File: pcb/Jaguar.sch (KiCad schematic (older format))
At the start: 52 parts

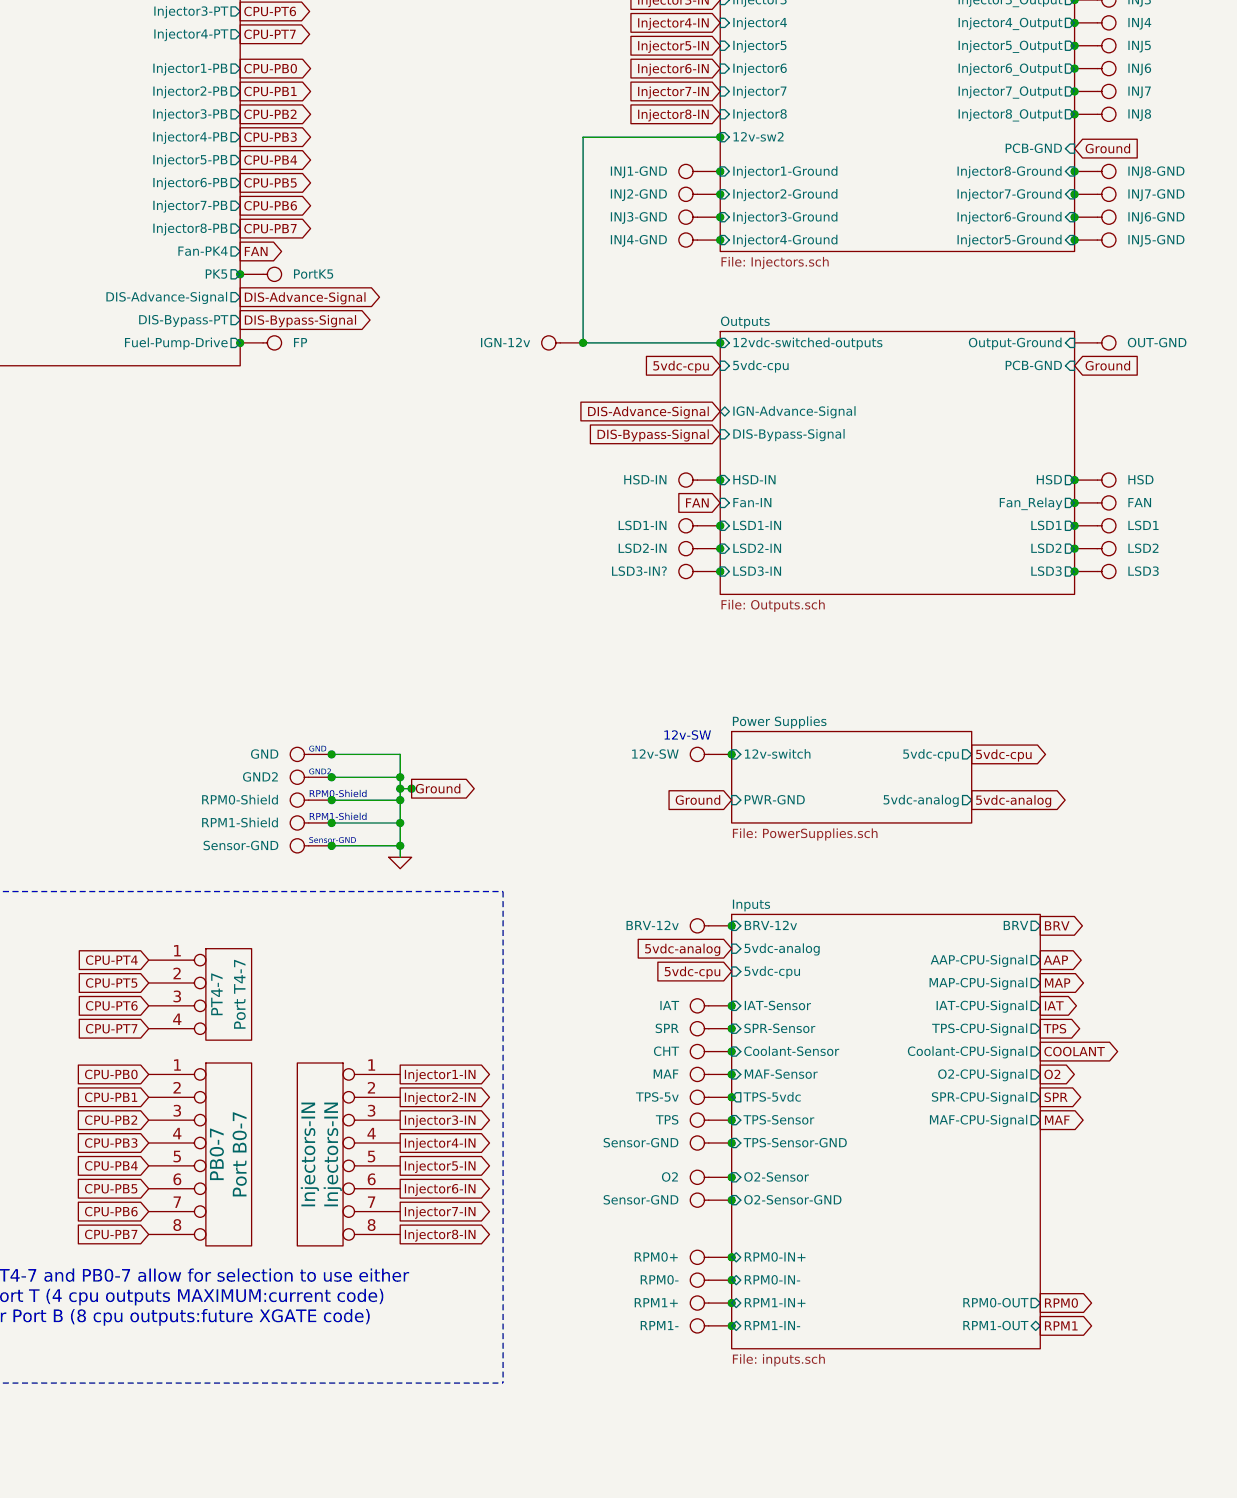
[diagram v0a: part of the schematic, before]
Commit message: Started laying out PCB changes for SO-8 high side driver and new SO-8 low side drivers.
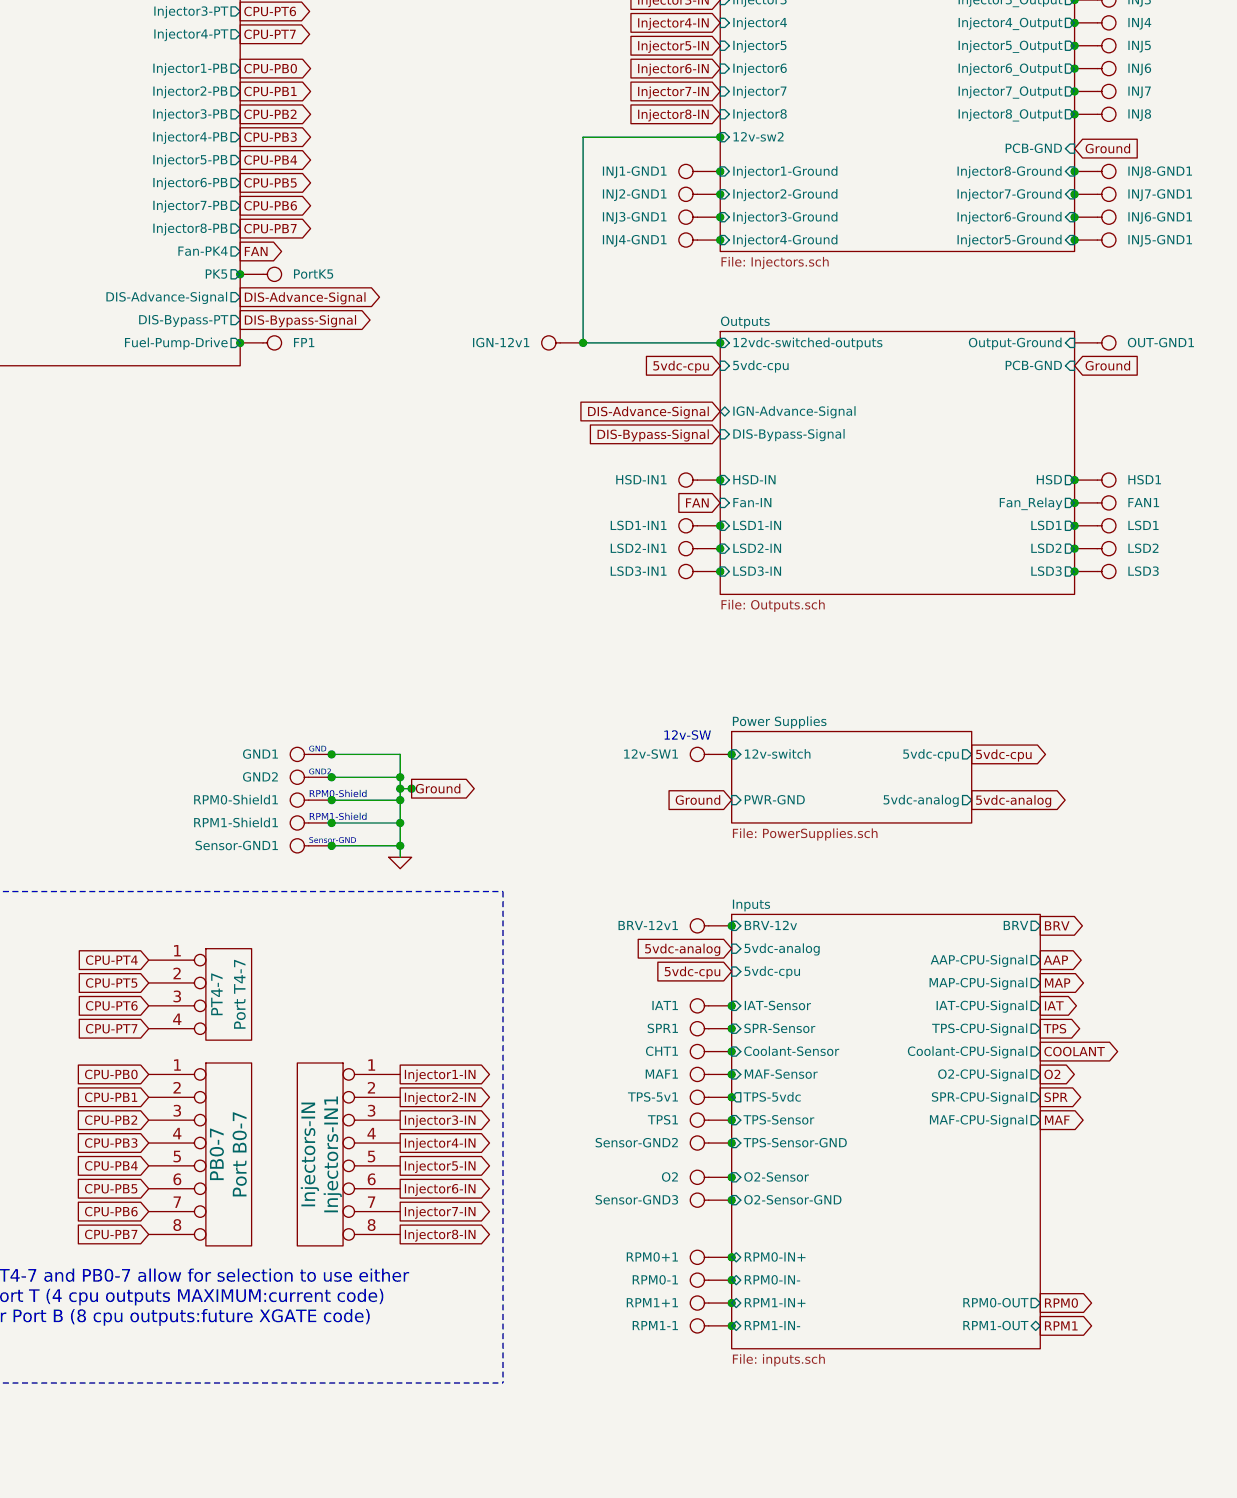
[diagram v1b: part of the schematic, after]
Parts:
- gave numbers to parts that had none: 1
- renumbered 12v-SW to 12v-SW1, BRV-12v to BRV-12v1, CHT to CHT1, FAN to FAN1, FP to FP1, GND to GND1, HSD-IN to HSD-IN1, HSD to HSD1, IAT to IAT1, IGN-12v to IGN-12v1, INJ1-GND to INJ1-GND1, INJ2-GND to INJ2-GND1, INJ3-GND to INJ3-GND1, INJ4-GND to INJ4-GND1, INJ5-GND to INJ5-GND1, INJ6-GND to INJ6-GND1, INJ7-GND to INJ7-GND1, INJ8-GND to INJ8-GND1, Injectors-IN to Injectors-IN1, LSD1-IN to LSD1-IN1, LSD2-IN to LSD2-IN1, MAF to MAF1, OUT-GND to OUT-GND1, RPM0+ to RPM0+1, RPM0- to RPM0-1, RPM0-Shield to RPM0-Shield1, RPM1+ to RPM1+1, RPM1- to RPM1-1, RPM1-Shield to RPM1-Shield1, SPR to SPR1, Sensor-GND to Sensor-GND1, Sensor-GND to Sensor-GND2, Sensor-GND to Sensor-GND3, TPS-5v to TPS-5v1, TPS to TPS1
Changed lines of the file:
@@
 Sheet 1 7
 Title "Jaguar PCB for FreeEMS"
-Date "5 feb 2014"
+Date "4 mar 2014"
 Rev "0.7-alpha"
 Comp "Git: xxxxxxxxxx"
@@
 MAF
 $Comp
-L CONN_1 INJ8-GND
+L CONN_1 INJ8-GND1
 U 1 1 4FF7159F
 P 10700 1650
-F 0 "INJ8-GND" H 10780 1650 40  0000 L CNN
+F 0 "INJ8-GND1" H 10780 1650 40  0000 L CNN
 F 1 "INJ8-GND" H 10700 1705 30  0001 C CNN
 F 2 "" H 10700 1650 60  0001 C CNN
@@
 $EndComp
 $Comp
-L CONN_1 INJ7-GND
+L CONN_1 INJ7-GND1
 U 1 1 4FF7159C
 P 10700 1750
-F 0 "INJ7-GND" H 10780 1750 40  0000 L CNN
+F 0 "INJ7-GND1" H 10780 1750 40  0000 L CNN
 F 1 "INJ7-GND" H 10700 1805 30  0001 C CNN
 F 2 "" H 10700 1750 60  0001 C CNN
@@
 $EndComp
 $Comp
-L CONN_1 INJ6-GND
+L CONN_1 INJ6-GND1
 U 1 1 4FF71599
 P 10700 1850
-F 0 "INJ6-GND" H 10780 1850 40  0000 L CNN
+F 0 "INJ6-GND1" H 10780 1850 40  0000 L CNN
 F 1 "INJ6-GND" H 10700 1905 30  0001 C CNN
 F 2 "" H 10700 1850 60  0001 C CNN
@@
 $EndComp
 $Comp
-L CONN_1 INJ5-GND
+L CONN_1 INJ5-GND1
 U 1 1 4FF71591
 P 10700 1950
-F 0 "INJ5-GND" H 10780 1950 40  0000 L CNN
+F 0 "INJ5-GND1" H 10780 1950 40  0000 L CNN
 F 1 "INJ5-GND" H 10700 2005 30  0001 C CNN
 F 2 "" H 10700 1950 60  0001 C CNN
@@
 $EndComp
 $Comp
-L CONN_1 INJ4-GND
+L CONN_1 INJ4-GND1
 U 1 1 4FF7158E
 P 8850 1950
-F 0 "INJ4-GND" H 8930 1950 40  0000 L CNN
+F 0 "INJ4-GND1" H 8930 1950 40  0000 L CNN
 F 1 "INJ4-GND" H 8850 2005 30  0001 C CNN
 F 2 "" H 8850 1950 60  0001 C CNN
@@
 $EndComp
 $Comp
-L CONN_1 INJ3-GND
+L CONN_1 INJ3-GND1
 U 1 1 4FF7158B
 P 8850 1850
-F 0 "INJ3-GND" H 8930 1850 40  0000 L CNN
+F 0 "INJ3-GND1" H 8930 1850 40  0000 L CNN
 F 1 "INJ3-GND" H 8850 1905 30  0001 C CNN
 F 2 "" H 8850 1850 60  0001 C CNN
@@
 5vdc-cpu = VDD\n\n5vdc-analog = VCC
 $Comp
-L CONN_1 Sensor-GND
+L CONN_1 Sensor-GND1
 U 1 1 4F2A0E57
 P 7150 4600
-F 0 "Sensor-GND" H 7230 4600 40  0000 L CNN
+F 0 "Sensor-GND1" H 7230 4600 40  0000 L CNN
 F 1 "Sensor-GND" H 7150 4655 30  0001 C CNN
 F 2 "" H 7150 4600 60  0001 C CNN
@@
 RPM0-Shield
 $Comp
-L CONN_1 RPM1-Shield
+L CONN_1 RPM1-Shield1
 U 1 1 4F2A0D57
 P 7150 4500
-F 0 "RPM1-Shield" H 7230 4500 40  0000 L CNN
+F 0 "RPM1-Shield1" H 7230 4500 40  0000 L CNN
 F 1 "RPM1-Shield" H 7150 4555 30  0001 C CNN
 F 2 "" H 7150 4500 60  0001 C CNN
@@
 $EndComp
 $Comp
-L CONN_1 RPM0-Shield
+L CONN_1 RPM0-Shield1
 U 1 1 4F2A0D4D
 P 7150 4400
-F 0 "RPM0-Shield" H 7230 4400 40  0000 L CNN
+F 0 "RPM0-Shield1" H 7230 4400 40  0000 L CNN
 F 1 "RPM0-Shield" H 7150 4455 30  0001 C CNN
 F 2 "" H 7150 4400 60  0001 C CNN
@@
 GND
 $Comp
-L CONN_1 INJ2-GND
+L CONN_1 INJ2-GND1
 U 1 1 4F2A047E
 P 8850 1750
-F 0 "INJ2-GND" H 8930 1750 40  0000 L CNN
+F 0 "INJ2-GND1" H 8930 1750 40  0000 L CNN
 F 1 "INJ2-GND" H 8850 1805 30  0001 C CNN
 F 2 "" H 8850 1750 60  0001 C CNN
@@
 $EndComp
 $Comp
-L CONN_1 MAF
+L CONN_1 MAF1
 U 1 1 4F22BF32
 P 8900 5600
-F 0 "MAF" H 8980 5600 40  0000 L CNN
+F 0 "MAF1" H 8980 5600 40  0000 L CNN
 F 1 "MAF" H 8900 5655 30  0001 C CNN
 F 2 "" H 8900 5600 60  0001 C CNN
@@
 $EndComp
 $Comp
-L CONN_1 LSD1-IN
+L CONN_1 LSD1-IN1
 U 1 1 4F2222E6
 P 8850 3200
-F 0 "LSD1-IN" H 8930 3200 40  0000 L CNN
+F 0 "LSD1-IN1" H 8930 3200 40  0000 L CNN
 F 1 "LSD1-IN" H 8850 3255 30  0001 C CNN
 F 2 "" H 8850 3200 60  0001 C CNN
@@
 $EndComp
 $Comp
-L CONN_1 LSD2-IN
+L CONN_1 LSD2-IN1
 U 1 1 4F2222DF
 P 8850 3300
-F 0 "LSD2-IN" H 8930 3300 40  0000 L CNN
+F 0 "LSD2-IN1" H 8930 3300 40  0000 L CNN
 F 1 "LSD2-IN" H 8850 3355 30  0001 C CNN
 F 2 "" H 8850 3300 60  0001 C CNN
@@
 Injector7-IN
 $Comp
-L CONN_8 Injectors-IN
+L CONN_8 Injectors-IN1
 U 1 1 4F20E01E
 P 7250 5950
-F 0 "Injectors-IN" V 7200 5950 60  0000 C CNN
+F 0 "Injectors-IN1" V 7200 5950 60  0000 C CNN
 F 1 "Injectors-IN" V 7300 5950 60  0000 C CNN
 F 2 "" H 7250 5950 60  0001 C CNN
@@
 Notes:
 $Comp
-L CONN_1 IGN-12v
+L CONN_1 IGN-12v1
 U 1 1 4F1CD4E4
 P 8250 2400
-F 0 "IGN-12v" H 8330 2400 40  0000 L CNN
+F 0 "IGN-12v1" H 8330 2400 40  0000 L CNN
 F 1 "IGN-12v" H 8250 2455 30  0001 C CNN
 F 2 "" H 8250 2400 60  0001 C CNN
@@
 $EndComp
 $Comp
-L CONN_1 OUT-GND
+L CONN_1 OUT-GND1
 U 1 1 4F1CD3BD
 P 10700 2400
-F 0 "OUT-GND" H 10780 2400 40  0000 L CNN
+F 0 "OUT-GND1" H 10780 2400 40  0000 L CNN
 F 1 "OUT-GND" H 10700 2455 30  0001 C CNN
 F 2 "" H 10700 2400 60  0001 C CNN
@@
 $EndComp
 $Comp
-L GND #PWR01
+L GND #PWR1
 U 1 1 4F1CCA54
 P 7600 4650
-F 0 "#PWR01" H 7600 4650 30  0001 C CNN
+F 0 "#PWR1" H 7600 4650 30  0001 C CNN
 F 1 "GND" H 7600 4580 30  0001 C CNN
 F 2 "" H 7600 4650 60  0001 C CNN
@@
 $EndComp
 $Comp
-L CONN_1 TPS-5v
+L CONN_1 TPS-5v1
 U 1 1 4F1CC8BD
 P 8900 5700
-F 0 "TPS-5v" H 8980 5700 40  0000 L CNN
+F 0 "TPS-5v1" H 8980 5700 40  0000 L CNN
 F 1 "TPS-5v" H 8900 5755 30  0001 C CNN
 F 2 "" H 8900 5700 60  0001 C CNN
@@
 5vdc-analog
 $Comp
-L CONN_1 GND
+L CONN_1 GND1
 U 1 1 4F189D7E
 P 7150 4200
-F 0 "GND" H 7230 4200 40  0000 L CNN
+F 0 "GND1" H 7230 4200 40  0000 L CNN
 F 1 "GND" H 7150 4255 30  0001 C CNN
 F 2 "" H 7150 4200 60  0001 C CNN
@@
 RPM1
 $Comp
-L CONN_1 RPM0-
+L CONN_1 RPM0-1
 U 1 1 4F186A57
 P 8900 6500
-F 0 "RPM0-" H 8980 6500 40  0000 L CNN
+F 0 "RPM0-1" H 8980 6500 40  0000 L CNN
 F 1 "RPM0-" H 8900 6555 30  0001 C CNN
 F 2 "" H 8900 6500 60  0001 C CNN
@@
 $EndComp
 $Comp
-L CONN_1 INJ1-GND
+L CONN_1 INJ1-GND1
 U 1 1 4F125936
 P 8850 1650
-F 0 "INJ1-GND" H 8930 1650 40  0000 L CNN
+F 0 "INJ1-GND1" H 8930 1650 40  0000 L CNN
 F 1 "INJ1-GND" H 8850 1705 30  0001 C CNN
 F 2 "" H 8850 1650 60  0001 C CNN
@@
 $EndComp
 $Comp
-L CONN_1 RPM1-
+L CONN_1 RPM1-1
 U 1 1 4F124A8E
 P 8900 6700
-F 0 "RPM1-" H 8980 6700 40  0000 L CNN
+F 0 "RPM1-1" H 8980 6700 40  0000 L CNN
 F 1 "RPM1-" H 8900 6755 30  0001 C CNN
 F 2 "" H 8900 6700 60  0001 C CNN
@@
 $EndComp
 $Comp
-L CONN_1 RPM1+
+L CONN_1 RPM1+1
 U 1 1 4F1248F4
 P 8900 6600
-F 0 "RPM1+" H 8980 6600 40  0000 L CNN
+F 0 "RPM1+1" H 8980 6600 40  0000 L CNN
 F 1 "RPM1+" H 8900 6655 30  0001 C CNN
 F 2 "" H 8900 6600 60  0001 C CNN
@@
 $EndComp
 $Comp
-L CONN_1 HSD
+L CONN_1 HSD1
 U 1 1 4F0D8467
 P 10700 3000
-F 0 "HSD" H 10780 3000 40  0000 L CNN
+F 0 "HSD1" H 10780 3000 40  0000 L CNN
 F 1 "FUEL" H 10700 3055 30  0001 C CNN
 F 2 "" H 10700 3000 60  0001 C CNN
@@
 $EndSheet
 $Comp
-L CONN_1 BRV-12v
+L CONN_1 BRV-12v1
 U 1 1 4F0C73A3
 P 8900 4950
-F 0 "BRV-12v" H 8980 4950 40  0000 L CNN
+F 0 "BRV-12v1" H 8980 4950 40  0000 L CNN
 F 1 "BRV-12v" H 8900 5005 30  0001 C CNN
 F 2 "" H 8900 4950 60  0001 C CNN
@@
 $EndComp
 $Comp
-L CONN_1 RPM0+
+L CONN_1 RPM0+1
 U 1 1 4F0BB599
 P 8900 6400
-F 0 "RPM0+" H 8980 6400 40  0000 L CNN
+F 0 "RPM0+1" H 8980 6400 40  0000 L CNN
 F 1 "RPM0+" H 8900 6455 30  0001 C CNN
 F 2 "" H 8900 6400 60  0001 C CNN
@@
 $EndComp
 $Comp
-L CONN_1 Sensor-GND
+L CONN_1 Sensor-GND3
 U 1 1 4F0BB588
 P 8900 6150
-F 0 "Sensor-GND" H 8980 6150 40  0000 L CNN
+F 0 "Sensor-GND3" H 8980 6150 40  0000 L CNN
 F 1 "Sensor-GND" H 8900 6205 30  0001 C CNN
 F 2 "" H 8900 6150 60  0001 C CNN
@@
 $EndComp
 $Comp
-L CONN_1 Sensor-GND
+L CONN_1 Sensor-GND2
 U 1 1 4F0BB568
 P 8900 5900
-F 0 "Sensor-GND" H 8980 5900 40  0000 L CNN
+F 0 "Sensor-GND2" H 8980 5900 40  0000 L CNN
 F 1 "Sensor-GND" H 8900 5955 30  0001 C CNN
 F 2 "" H 8900 5900 60  0001 C CNN
@@
 $EndComp
 $Comp
-L CONN_1 TPS
+L CONN_1 TPS1
 U 1 1 4F0BB55E
 P 8900 5800
-F 0 "TPS" H 8980 5800 40  0000 L CNN
+F 0 "TPS1" H 8980 5800 40  0000 L CNN
 F 1 "TPS" H 8900 5855 30  0001 C CNN
 F 2 "" H 8900 5800 60  0001 C CNN
@@
 $EndComp
 $Comp
-L CONN_1 CHT
+L CONN_1 CHT1
 U 1 1 4F0BB53F
 P 8900 5500
-F 0 "CHT" H 8980 5500 40  0000 L CNN
+F 0 "CHT1" H 8980 5500 40  0000 L CNN
 F 1 "CHT" H 8900 5555 30  0001 C CNN
 F 2 "" H 8900 5500 60  0001 C CNN
@@
 $EndComp
 $Comp
-L CONN_1 SPR
+L CONN_1 SPR1
 U 1 1 4F0BB535
 P 8900 5400
-F 0 "SPR" H 8980 5400 40  0000 L CNN
+F 0 "SPR1" H 8980 5400 40  0000 L CNN
 F 1 "SPR" H 8900 5455 30  0001 C CNN
 F 2 "" H 8900 5400 60  0001 C CNN
@@
 $EndComp
 $Comp
-L CONN_1 IAT
+L CONN_1 IAT1
 U 1 1 4F0BB528
 P 8900 5300
-F 0 "IAT" H 8980 5300 40  0000 L CNN
+F 0 "IAT1" H 8980 5300 40  0000 L CNN
 F 1 "IAT" H 8900 5355 30  0001 C CNN
 F 2 "" H 8900 5300 60  0001 C CNN
@@
 5vdc-analog
 $Comp
-L CONN_1 12v-SW
+L CONN_1 12v-SW1
 U 1 1 4F0A55A0
 P 8900 4200
-F 0 "12v-SW" H 8980 4200 40  0000 L CNN
+F 0 "12v-SW1" H 8980 4200 40  0000 L CNN
 F 1 "12v-SW" H 8900 4255 30  0001 C CNN
 F 2 "" H 8900 4200 60  0001 C CNN
@@
 	5650 4800 5650 6950
 $Comp
-L CONN_1 FP
+L CONN_1 FP1
 U 1 1 52F28E03
 P 7050 2400
-F 0 "FP" H 7130 2400 40  0000 L CNN
+F 0 "FP1" H 7130 2400 40  0000 L CNN
 F 1 "FP" H 7050 2455 30  0001 C CNN
 F 2 "" H 7050 2400 60  0001 C CNN
@@
 $EndComp
 $Comp
-L CONN_1 HSD-IN
+L CONN_1 HSD-IN1
 U 1 1 52F2A6F9
 P 8850 3000
-F 0 "HSD-IN" H 8930 3000 40  0000 L CNN
+F 0 "HSD-IN1" H 8930 3000 40  0000 L CNN
 F 1 "HSD-IN" H 8850 3055 30  0001 C CNN
 F 2 "" H 8850 3000 60  0001 C CNN
@@
 Connection ~ 9050 6700
 $Comp
-L CONN_1 LSD3-IN?
+L CONN_1 LSD3-IN1
 U 1 1 52F37A7E
 P 8850 3400
-F 0 "LSD3-IN?" H 8930 3400 40  0000 L CNN
+F 0 "LSD3-IN1" H 8930 3400 40  0000 L CNN
 F 1 "LSD2-IN" H 8850 3455 30  0001 C CNN
 F 2 "" H 8850 3400 60  0001 C CNN
@@
 $EndComp
 $Comp
-L CONN_1 FAN
+L CONN_1 FAN1
 U 1 1 52F3899C
 P 10700 3100
-F 0 "FAN" H 10780 3100 40  0000 L CNN
+F 0 "FAN1" H 10780 3100 40  0000 L CNN
 F 1 "FAN" H 10700 3155 30  0001 C CNN
 F 2 "" H 10700 3100 60  0001 C CNN

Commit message: Initial layout of high side driver on PCB complete.
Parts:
- HSD1: value FUEL -> HSD
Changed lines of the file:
@@
 Sheet 1 7
 Title "Jaguar PCB for FreeEMS"
-Date "4 mar 2014"
+Date "5 mar 2014"
 Rev "0.7-alpha"
 Comp "Git: xxxxxxxxxx"
@@
 P 10700 3000
 F 0 "HSD1" H 10780 3000 40  0000 L CNN
-F 1 "FUEL" H 10700 3055 30  0001 C CNN
+F 1 "HSD" H 10700 3055 30  0001 C CNN
 F 2 "" H 10700 3000 60  0001 C CNN
 F 3 "" H 10700 3000 60  0001 C CNN

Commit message: Finished placement and routing of low side drivers on PCB, ran DRC and found no errors.
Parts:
- LSD3: value LSD2 -> LSD3
- LSD3-IN1: value LSD2-IN -> LSD3-IN
- OUT-GND1: value OUT-GND -> OUTPUT-GND
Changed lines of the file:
@@
 Sheet 1 7
 Title "Jaguar PCB for FreeEMS"
-Date "5 mar 2014"
+Date "6 mar 2014"
 Rev "0.7-alpha"
 Comp "Git: xxxxxxxxxx"
@@
 P 10700 2400
 F 0 "OUT-GND1" H 10780 2400 40  0000 L CNN
-F 1 "OUT-GND" H 10700 2455 30  0001 C CNN
+F 1 "OUTPUT-GND" H 10700 2455 30  0001 C CNN
 F 2 "" H 10700 2400 60  0001 C CNN
 F 3 "" H 10700 2400 60  0001 C CNN
@@
 $EndComp
 $Comp
-L GND #PWR1
+L GND #PWR01
 U 1 1 4F1CCA54
 P 7600 4650
-F 0 "#PWR1" H 7600 4650 30  0001 C CNN
+F 0 "#PWR01" H 7600 4650 30  0001 C CNN
 F 1 "GND" H 7600 4580 30  0001 C CNN
 F 2 "" H 7600 4650 60  0001 C CNN
@@
 P 8850 3400
 F 0 "LSD3-IN1" H 8930 3400 40  0000 L CNN
-F 1 "LSD2-IN" H 8850 3455 30  0001 C CNN
+F 1 "LSD3-IN" H 8850 3455 30  0001 C CNN
 F 2 "" H 8850 3400 60  0001 C CNN
 F 3 "" H 8850 3400 60  0001 C CNN
@@
 P 10700 3400
 F 0 "LSD3" H 10780 3400 40  0000 L CNN
-F 1 "LSD2" H 10700 3455 30  0001 C CNN
+F 1 "LSD3" H 10700 3455 30  0001 C CNN
 F 2 "" H 10700 3400 60  0001 C CNN
 F 3 "" H 10700 3400 60  0001 C CNN
